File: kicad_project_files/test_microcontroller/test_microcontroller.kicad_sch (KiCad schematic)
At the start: 40 parts, among them J1 USB_C_Receptacle_USB2.0, SW1 SW_Push, SW2 SW_Push, SW3 SW_Push, SW4 SW_Push, SW5 SW_Push, SW6 SW_Push, SW7 SW_Push, SW8 SW_Push, SW9 SW_Push, U1 ATmega32U4-A, Y1 16mhz

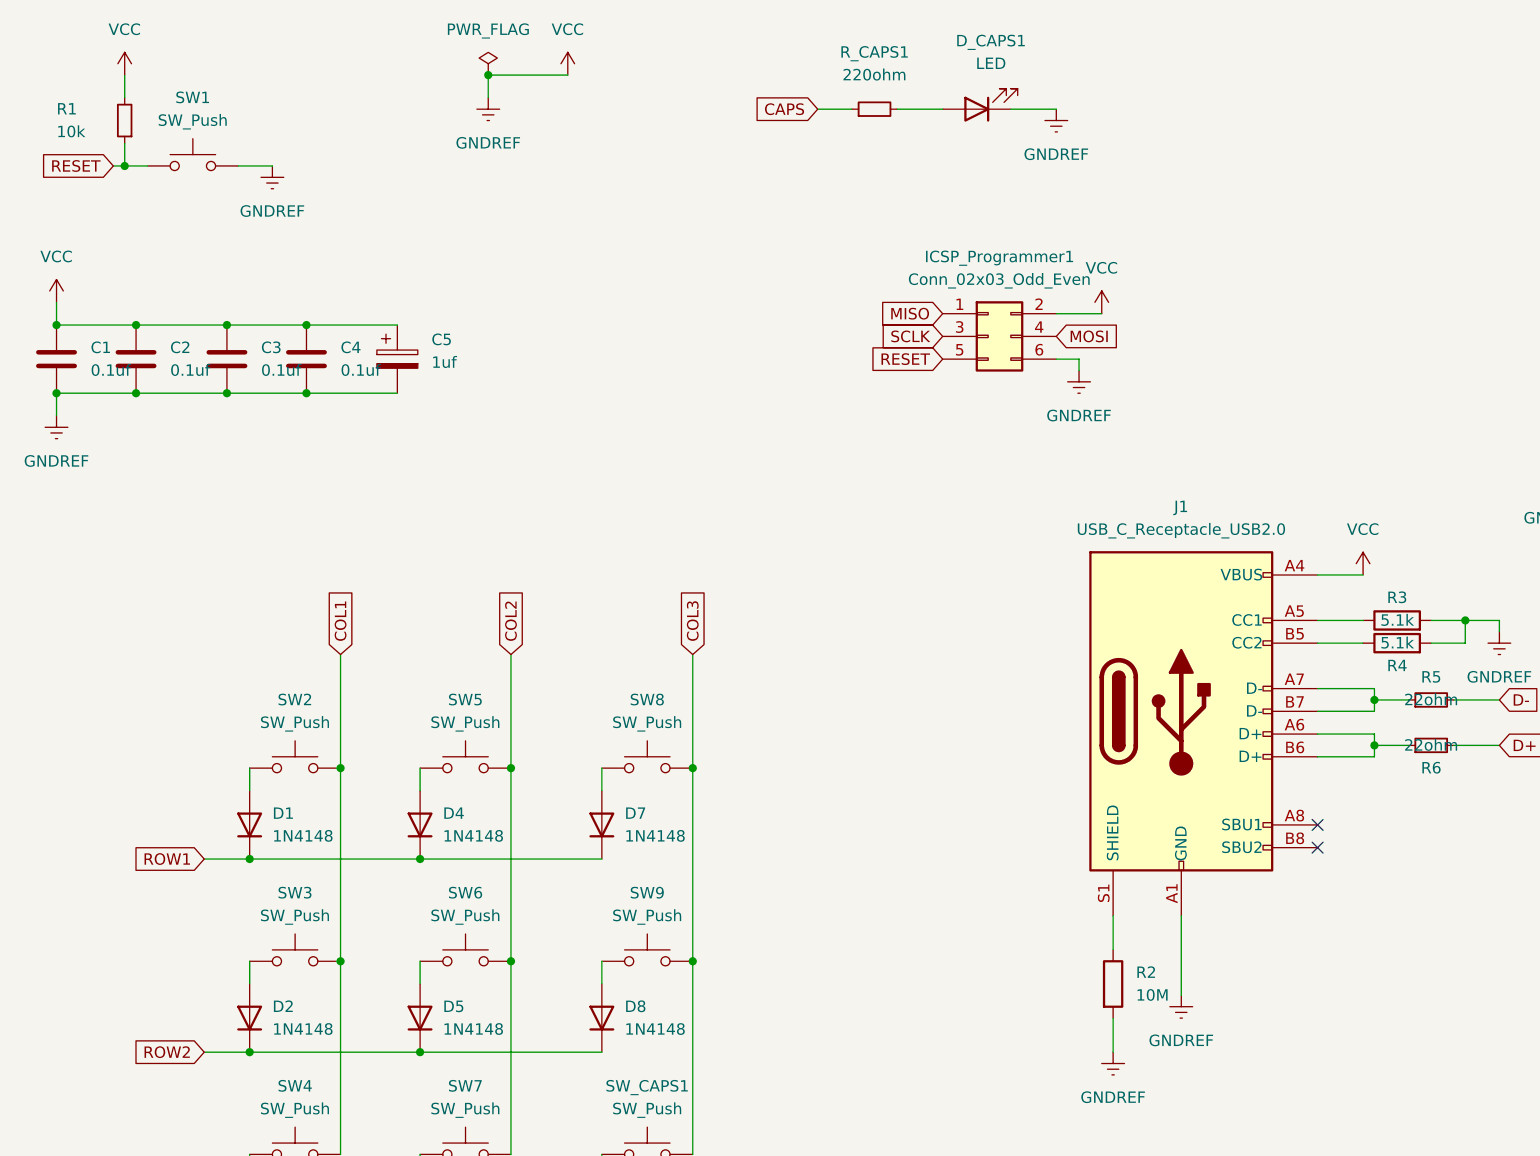
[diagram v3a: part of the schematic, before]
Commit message: add traces to pcb
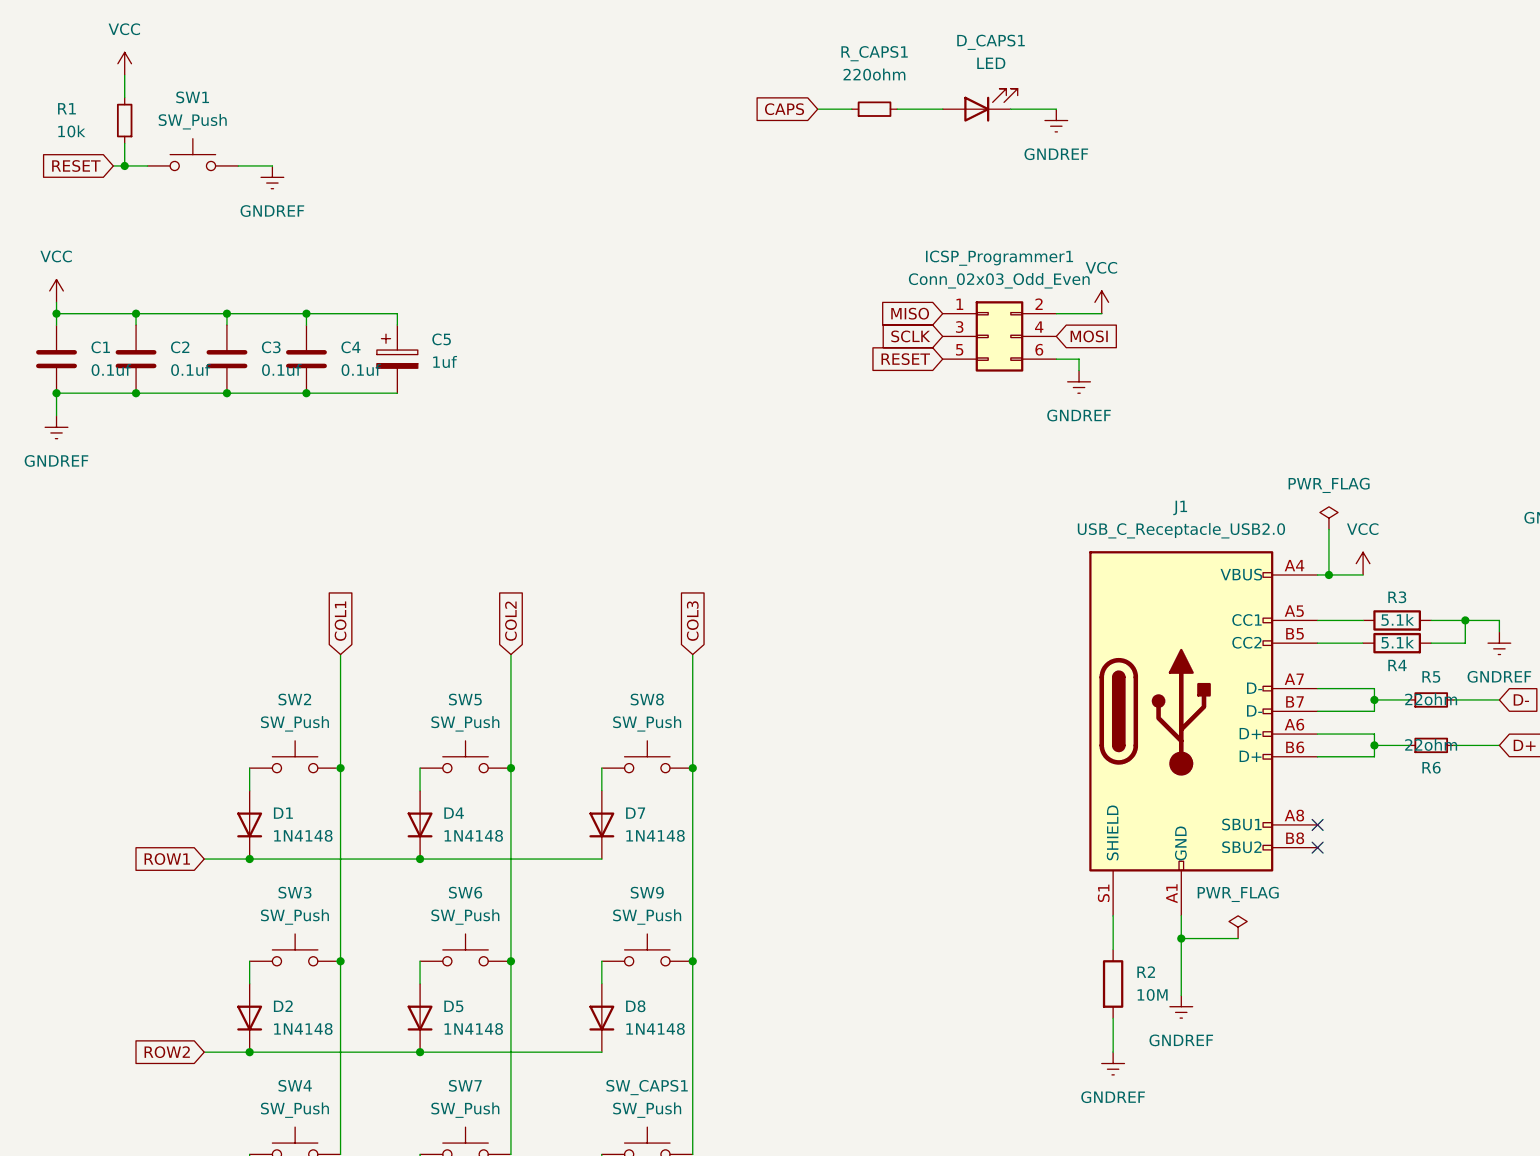
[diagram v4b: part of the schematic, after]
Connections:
- net GNDREF: no longer C1.1, C2.1, C3.1, C4.1, C5.1, ICSP_Programmer1.2 (Pin_2), J1.A4 (VBUS), J1.A9 (VBUS), J1.B4 (VBUS), J1.B9 (VBUS), R1.2, U1.14 (VCC), U1.2 (UVCC), U1.24 (AVCC), U1.34 (VCC), U1.44 (AVCC), U1.7 (VBUS)
- new net VCC: C1.1, C2.1, C3.1, C4.1, C5.1, ICSP_Programmer1.2 (Pin_2), J1.A4 (VBUS), J1.A9 (VBUS), J1.B4 (VBUS), J1.B9 (VBUS), R1.2, U1.14 (VCC), U1.2 (UVCC), U1.24 (AVCC), U1.34 (VCC), U1.44 (AVCC), U1.7 (VBUS)
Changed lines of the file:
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@@
   (junction (at 67.31 96.52) (diameter 0) (color 0 0 0 0)
   )
-  (junction (at 25.4 46.99) (diameter 0) (color 0 0 0 0)
+  (junction (at 25.4 45.72) (diameter 0) (color 0 0 0 0)
   )
   (junction (at 204.47 53.34) (diameter 0) (color 0 0 0 0)
@@
   (junction (at 173.99 80.01) (diameter 0) (color 0 0 0 0)
   )
-  (junction (at 64.77 19.05) (diameter 0) (color 0 0 0 0)
-  )
   (junction (at 25.4 54.61) (diameter 0) (color 0 0 0 0)
   )
@@
   (junction (at 229.87 138.43) (diameter 0) (color 0 0 0 0)
   )
+  (junction (at 142.24 115.57) (diameter 0) (color 0 0 0 0)
+  )
   (junction (at 38.1 149.86) (diameter 0) (color 0 0 0 0)
   )
@@
   (junction (at 57.15 149.86) (diameter 0) (color 0 0 0 0)
   )
-  (junction (at 35.56 46.99) (diameter 0) (color 0 0 0 0)
+  (junction (at 35.56 45.72) (diameter 0) (color 0 0 0 0)
   )
   (junction (at 38.1 128.27) (diameter 0) (color 0 0 0 0)
   )
-  (junction (at 44.45 46.99) (diameter 0) (color 0 0 0 0)
+  (junction (at 44.45 45.72) (diameter 0) (color 0 0 0 0)
   )
   (junction (at 67.31 118.11) (diameter 0) (color 0 0 0 0)
@@
   (junction (at 38.1 106.68) (diameter 0) (color 0 0 0 0)
   )
-  (junction (at 16.51 46.99) (diameter 0) (color 0 0 0 0)
+  (junction (at 16.51 45.72) (diameter 0) (color 0 0 0 0)
+  )
+  (junction (at 158.75 74.93) (diameter 0) (color 0 0 0 0)
   )
   (junction (at 48.26 96.52) (diameter 0) (color 0 0 0 0)
@@
     (stroke (width 0) (type default) (color 0 0 0 0))
   )
-  (wire (pts (xy 35.56 46.99) (xy 44.45 46.99))
+  (wire (pts (xy 35.56 45.72) (xy 44.45 45.72))
+    (stroke (width 0) (type default) (color 0 0 0 0))
+  )
+  (wire (pts (xy 158.75 74.93) (xy 162.56 74.93))
     (stroke (width 0) (type default) (color 0 0 0 0))
   )
@@
     (stroke (width 0) (type default) (color 0 0 0 0))
   )
+  (wire (pts (xy 25.4 45.72) (xy 25.4 46.99))
+    (stroke (width 0) (type default) (color 0 0 0 0))
+  )
   (wire (pts (xy 177.8 80.01) (xy 177.8 81.28))
     (stroke (width 0) (type default) (color 0 0 0 0))
   )
-  (wire (pts (xy 64.77 19.05) (xy 64.77 21.59))
+  (wire (pts (xy 158.75 69.85) (xy 158.75 74.93))
     (stroke (width 0) (type default) (color 0 0 0 0))
   )
@@
     (stroke (width 0) (type default) (color 0 0 0 0))
   )
-  (wire (pts (xy 142.24 113.03) (xy 142.24 121.92))
+  (wire (pts (xy 142.24 113.03) (xy 142.24 115.57))
     (stroke (width 0) (type default) (color 0 0 0 0))
   )
@@
     (stroke (width 0) (type default) (color 0 0 0 0))
   )
-  (wire (pts (xy 44.45 46.99) (xy 54.61 46.99))
+  (wire (pts (xy 44.45 45.72) (xy 54.61 45.72))
     (stroke (width 0) (type default) (color 0 0 0 0))
   )
@@
     (stroke (width 0) (type default) (color 0 0 0 0))
   )
-  (wire (pts (xy 25.4 46.99) (xy 35.56 46.99))
+  (wire (pts (xy 25.4 45.72) (xy 35.56 45.72))
     (stroke (width 0) (type default) (color 0 0 0 0))
   )
@@
     (stroke (width 0) (type default) (color 0 0 0 0))
   )
-  (wire (pts (xy 16.51 46.99) (xy 25.4 46.99))
+  (wire (pts (xy 16.51 45.72) (xy 25.4 45.72))
     (stroke (width 0) (type default) (color 0 0 0 0))
   )
@@
     (stroke (width 0) (type default) (color 0 0 0 0))
   )
+  (wire (pts (xy 35.56 45.72) (xy 35.56 46.99))
+    (stroke (width 0) (type default) (color 0 0 0 0))
+  )
   (wire (pts (xy 163.83 90.17) (xy 163.83 88.9))
     (stroke (width 0) (type default) (color 0 0 0 0))
@@
     (stroke (width 0) (type default) (color 0 0 0 0))
   )
+  (wire (pts (xy 142.24 115.57) (xy 148.59 115.57))
+    (stroke (width 0) (type default) (color 0 0 0 0))
+  )
   (wire (pts (xy 214.63 60.96) (xy 204.47 60.96))
     (stroke (width 0) (type default) (color 0 0 0 0))
@@
     (stroke (width 0) (type default) (color 0 0 0 0))
   )
-  (wire (pts (xy 157.48 74.93) (xy 162.56 74.93))
+  (wire (pts (xy 157.48 74.93) (xy 158.75 74.93))
     (stroke (width 0) (type default) (color 0 0 0 0))
   )
@@
     (stroke (width 0) (type default) (color 0 0 0 0))
   )
-  (wire (pts (xy 64.77 19.05) (xy 73.66 19.05))
-    (stroke (width 0) (type default) (color 0 0 0 0))
-  )
   (wire (pts (xy 184.15 53.34) (xy 184.15 60.96))
     (stroke (width 0) (type default) (color 0 0 0 0))
@@
     (stroke (width 0) (type default) (color 0 0 0 0))
   )
+  (wire (pts (xy 142.24 115.57) (xy 142.24 121.92))
+    (stroke (width 0) (type default) (color 0 0 0 0))
+  )
   (wire (pts (xy 87.63 96.52) (xy 87.63 118.11))
     (stroke (width 0) (type default) (color 0 0 0 0))
@@
     (stroke (width 0) (type default) (color 0 0 0 0))
   )
+  (wire (pts (xy 16.51 45.72) (xy 16.51 46.99))
+    (stroke (width 0) (type default) (color 0 0 0 0))
+  )
   (wire (pts (xy 157.48 82.55) (xy 162.56 82.55))
     (stroke (width 0) (type default) (color 0 0 0 0))
@@
     (stroke (width 0) (type default) (color 0 0 0 0))
   )
+  (wire (pts (xy 44.45 45.72) (xy 44.45 46.99))
+    (stroke (width 0) (type default) (color 0 0 0 0))
+  )
   (wire (pts (xy 77.47 118.11) (xy 77.47 120.65))
     (stroke (width 0) (type default) (color 0 0 0 0))
@@
     (stroke (width 0) (type default) (color 0 0 0 0))
   )
+  (wire (pts (xy 54.61 45.72) (xy 54.61 46.99))
+    (stroke (width 0) (type default) (color 0 0 0 0))
+  )
   (wire (pts (xy 24.13 29.21) (xy 26.67 29.21))
     (stroke (width 0) (type default) (color 0 0 0 0))
@@
     (stroke (width 0) (type default) (color 0 0 0 0))
   )
-  (wire (pts (xy 16.51 44.45) (xy 16.51 46.99))
+  (wire (pts (xy 16.51 44.45) (xy 16.51 45.72))
     (stroke (width 0) (type default) (color 0 0 0 0))
   )
@@
     (pin "2")
   )
+  (symbol (lib_id "power:PWR_FLAG") (at 148.59 115.57 0) (unit 1)
+    (in_bom yes) (on_board yes) (fields_autoplaced)
+    (property "Reference" "#FLG?" (id 0) (at 148.59 113.665 0)
+      (effects (font (size 1.27 1.27)) hide)
+    )
+    (property "Value" "PWR_FLAG" (id 1) (at 148.59 110.49 0))
+    (property "Footprint" "" (id 2) (at 148.59 115.57 0)
+      (effects (font (size 1.27 1.27)) hide)
+    )
+    (property "Datasheet" "~" (id 3) (at 148.59 115.57 0)
+      (effects (font (size 1.27 1.27)) hide)
+    )
+    (pin "1")
+  )
   (symbol (lib_id "Device:C") (at 16.51 50.8 0) (unit 1)
     (in_bom yes) (on_board yes) (fields_autoplaced)
@@
     (pin "2")
   )
-  (symbol (lib_id "power:VCC") (at 73.66 19.05 0) (unit 1)
-    (in_bom yes) (on_board yes) (fields_autoplaced)
-    (property "Reference" "#PWR0102" (id 0) (at 73.66 22.86 0)
-      (effects (font (size 1.27 1.27)) hide)
-    )
-    (property "Value" "VCC" (id 1) (at 73.66 13.97 0))
-    (property "Footprint" "" (id 2) (at 73.66 19.05 0)
-      (effects (font (size 1.27 1.27)) hide)
-    )
-    (property "Datasheet" "" (id 3) (at 73.66 19.05 0)
-      (effects (font (size 1.27 1.27)) hide)
-    )
-    (pin "1")
-  )
   (symbol (lib_id "power:GNDREF") (at 134.62 128.27 0) (unit 1)
     (in_bom yes) (on_board yes) (fields_autoplaced)
@@
     (pin "1")
     (pin "2")
+  )
+  (symbol (lib_id "power:PWR_FLAG") (at 158.75 69.85 0) (unit 1)
+    (in_bom yes) (on_board yes) (fields_autoplaced)
+    (property "Reference" "#FLG?" (id 0) (at 158.75 67.945 0)
+      (effects (font (size 1.27 1.27)) hide)
+    )
+    (property "Value" "PWR_FLAG" (id 1) (at 158.75 64.77 0))
+    (property "Footprint" "" (id 2) (at 158.75 69.85 0)
+      (effects (font (size 1.27 1.27)) hide)
+    )
+    (property "Datasheet" "~" (id 3) (at 158.75 69.85 0)
+      (effects (font (size 1.27 1.27)) hide)
+    )
+    (pin "1")
   )
   (symbol (lib_id "Switch:SW_Push") (at 62.23 118.11 0) (unit 1)
@@
     (pin "2")
   )
-  (symbol (lib_id "power:PWR_FLAG") (at 64.77 19.05 0) (unit 1)
-    (in_bom yes) (on_board yes) (fields_autoplaced)
-    (property "Reference" "#FLG0101" (id 0) (at 64.77 17.145 0)
-      (effects (font (size 1.27 1.27)) hide)
-    )
-    (property "Value" "PWR_FLAG" (id 1) (at 64.77 13.97 0))
-    (property "Footprint" "" (id 2) (at 64.77 19.05 0)
-      (effects (font (size 1.27 1.27)) hide)
-    )
-    (property "Datasheet" "~" (id 3) (at 64.77 19.05 0)
-      (effects (font (size 1.27 1.27)) hide)
-    )
-    (pin "1")
-  )
   (symbol (lib_id "Device:C") (at 35.56 50.8 0) (unit 1)
     (in_bom yes) (on_board yes) (fields_autoplaced)
@@
     (pin "1")
     (pin "2")
-  )
-  (symbol (lib_id "power:GNDREF") (at 64.77 21.59 0) (unit 1)
-    (in_bom yes) (on_board yes) (fields_autoplaced)
-    (property "Reference" "#PWR015" (id 0) (at 64.77 27.94 0)
-      (effects (font (size 1.27 1.27)) hide)
-    )
-    (property "Value" "GNDREF" (id 1) (at 64.77 26.67 0))
-    (property "Footprint" "" (id 2) (at 64.77 21.59 0)
-      (effects (font (size 1.27 1.27)) hide)
-    )
-    (property "Datasheet" "" (id 3) (at 64.77 21.59 0)
-      (effects (font (size 1.27 1.27)) hide)
-    )
-    (pin "1")
   )
   (symbol (lib_id "Device:R_Small") (at 170.18 93.98 90) (unit 1)
@@
   )
   (symbol_instances
-    (path "/dce62fa6-8e66-4e77-9956-fbef1b854de8"
-      (reference "#FLG0101") (unit 1) (value "PWR_FLAG") (footprint "")
+    (path "/4d3913c1-6eaf-4788-b16d-404de55aea6d"
+      (reference "#FLG?") (unit 1) (value "PWR_FLAG") (footprint "")
+    )
+    (path "/910bf9c7-3f9b-4ebb-810c-f11944d95f58"
+      (reference "#FLG?") (unit 1) (value "PWR_FLAG") (footprint "")
     )
     (path "/51f6aabe-8284-47cf-8ddc-0d885dfc999b"
@@
       (reference "#PWR014") (unit 1) (value "GNDREF") (footprint "")
     )
-    (path "/f70e8927-2299-449c-b52c-553c1bc34b5d"
-      (reference "#PWR015") (unit 1) (value "GNDREF") (footprint "")
-    )
     (path "/6f9440f8-a9f0-42af-bfc6-f816927170e2"
       (reference "#PWR016") (unit 1) (value "GNDREF") (footprint "")
@@
       (reference "#PWR0101") (unit 1) (value "GNDREF") (footprint "")
     )
-    (path "/7a82b3b6-fdb1-43e5-b4c5-ae0f7d6a869d"
-      (reference "#PWR0102") (unit 1) (value "VCC") (footprint "")
-    )
     (path "/4d48e41d-3878-4a27-ab4f-51a7ebfea6fe"
